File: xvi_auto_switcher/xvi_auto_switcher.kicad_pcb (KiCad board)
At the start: 2 copper layers, 45 x 102 mm, 20 parts, among them J1 DB37_Female_MountingHoles, J2 Conn_02x17_Odd_Even, J3 Conn_02x17_Odd_Even, J4 Conn_01x04_Male, J5 Conn_01x02_Male, U1 74LS157, U2 74LS07

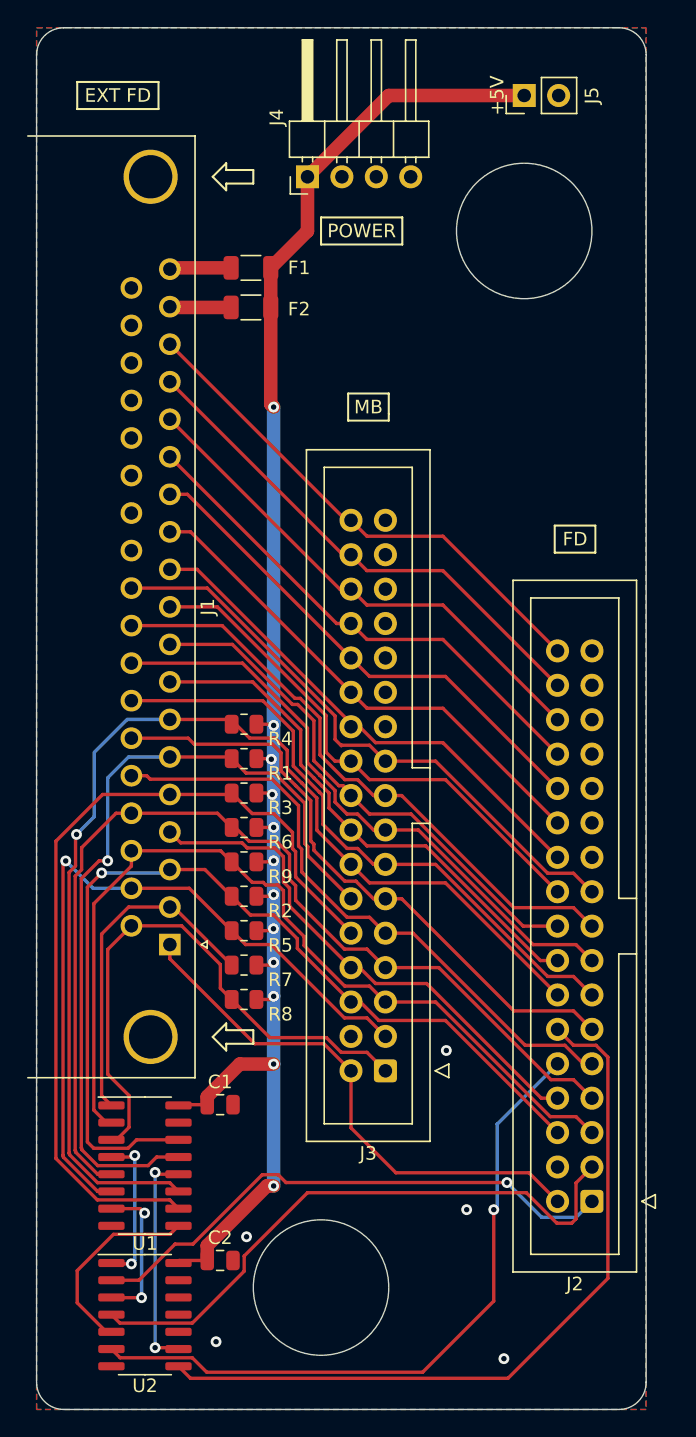
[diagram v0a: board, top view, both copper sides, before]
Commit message: update auto switcher pcb connector positions and add caps
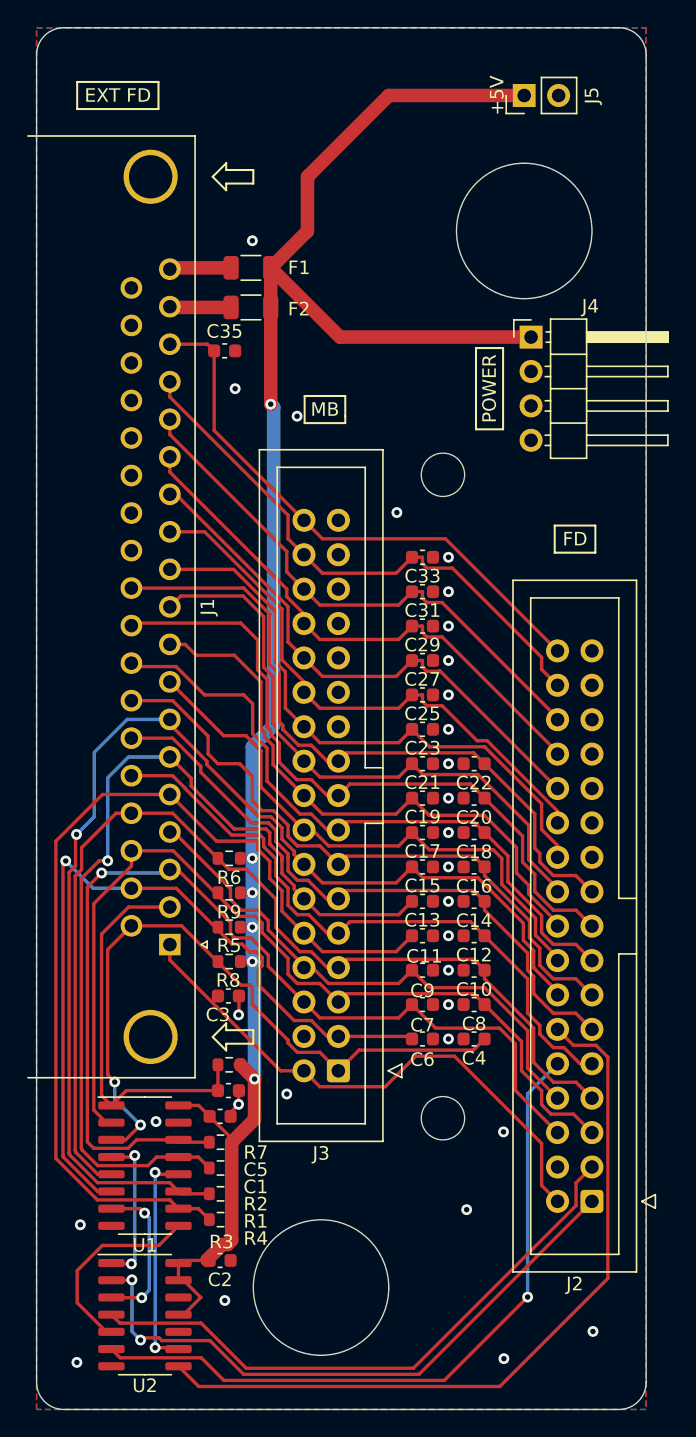
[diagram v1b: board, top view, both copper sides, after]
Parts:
- added C10: 47p, Capacitor_SMD:C_0603_1608Metric, F.Cu at (132.3, 129.6)
- added C11: 47p, Capacitor_SMD:C_0603_1608Metric, F.Cu at (128.5, 127.0)
- added C12: 47p, Capacitor_SMD:C_0603_1608Metric, F.Cu at (132.3, 127.0)
- added C13: 47p, Capacitor_SMD:C_0603_1608Metric, F.Cu at (128.5, 124.5)
- added C14: 47p, Capacitor_SMD:C_0603_1608Metric, F.Cu at (132.3, 124.5)
- added C15: 47p, Capacitor_SMD:C_0603_1608Metric, F.Cu at (128.5, 122.0)
- added C16: 47p, Capacitor_SMD:C_0603_1608Metric, F.Cu at (132.3, 122.0)
- added C17: 47p, Capacitor_SMD:C_0603_1608Metric, F.Cu at (128.5, 119.4)
- added C18: 47p, Capacitor_SMD:C_0603_1608Metric, F.Cu at (132.3, 119.4)
- added C19: 47p, Capacitor_SMD:C_0603_1608Metric, F.Cu at (128.5, 116.9)
- added C20: 47p, Capacitor_SMD:C_0603_1608Metric, F.Cu at (132.3, 116.9)
- added C21: 47p, Capacitor_SMD:C_0603_1608Metric, F.Cu at (128.5, 114.3)
- added C22: 47p, Capacitor_SMD:C_0603_1608Metric, F.Cu at (132.3, 114.3)
- added C23: 47p, Capacitor_SMD:C_0603_1608Metric, F.Cu at (128.5, 111.8)
- added C25: 47p, Capacitor_SMD:C_0603_1608Metric, F.Cu at (128.5, 109.2)
- added C27: 47p, Capacitor_SMD:C_0603_1608Metric, F.Cu at (128.5, 106.7)
- added C29: 47p, Capacitor_SMD:C_0603_1608Metric, F.Cu at (128.5, 104.2)
- added C3: 47p, Capacitor_SMD:C_0603_1608Metric, F.Cu at (114.2, 131.5)
- added C31: 47p, Capacitor_SMD:C_0603_1608Metric, F.Cu at (128.5, 101.6)
- added C33: 47p, Capacitor_SMD:C_0603_1608Metric, F.Cu at (128.5, 99.1)
- added C35: 47p, Capacitor_SMD:C_0603_1608Metric, F.Cu at (113.9, 83.8)
- added C4: 47p, Capacitor_SMD:C_0603_1608Metric, F.Cu at (132.3, 134.7)
- added C5: 47p, Capacitor_SMD:C_0603_1608Metric, F.Cu at (114.2, 138.5)
- added C6: 47p, Capacitor_SMD:C_0603_1608Metric, F.Cu at (128.5, 134.7)
- added C7: 47p, Capacitor_SMD:C_0603_1608Metric, F.Cu at (128.5, 132.1)
- added C8: 47p, Capacitor_SMD:C_0603_1608Metric, F.Cu at (132.3, 132.1)
- added C9: 47p, Capacitor_SMD:C_0603_1608Metric, F.Cu at (128.5, 129.6)
- added REF**: MountingHole_3.2mm_M3, MountingHole:MountingHole_3.2mm_M3, F.Cu at (130.0, 140.5)
- added REF**: MountingHole_3.2mm_M3, MountingHole:MountingHole_3.2mm_M3, F.Cu at (130.0, 93.0)
- C1, C2: footprint Capacitor_SMD:C_0805_2012Metric -> Capacitor_SMD:C_0603_1608Metric
- R1, R2, R3, R4, R5, R6, R7, R8, R9: footprint Resistor_SMD:R_0805_2012Metric -> Resistor_SMD:R_0603_1608Metric
- moved R4 34.7 mm to (113.6, 146.1)
- moved R3 31.5 mm to (113.6, 148.0)
- moved R1 30.3 mm to (113.6, 144.2)
- moved J4 20.3 mm to (136.5, 82.8), turned to 0 degrees
- moved R2 18.2 mm to (113.6, 142.3)
- moved R7 7.44 mm to (114.2, 136.6)
- moved J3 3.47 mm to (122.3, 137.0)
- moved R8 3.01 mm to (114.2, 128.9)
- moved R6 2.53 mm to (114.2, 121.3)
- moved R9 2.53 mm to (114.2, 123.9)
- moved R5 1.13 mm to (114.2, 126.4)
- moved C1 0.87 mm to (113.5, 140.4)
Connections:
- U2 pad 10: (no net) -> unconnected-(U2-Pad10)
- U2 pad 11: (no net) -> +5V
- U2 pad 12: (no net) -> unconnected-(U2-Pad12)
- U2 pad 13: (no net) -> +5V
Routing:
- net +5V: track 125.9 -> 141.4 mm, vias 12 -> 6
- net /~{OPTION0}: track 42.1 -> 51.4 mm, vias 0 -> 2
- net /~{DS0}: track 63.4 -> 71.6 mm
- net /~{DS1}: track 61.6 -> 69.2 mm
- net /~{WDATA}: track 37.6 -> 43.6 mm
- net /~{STEP}: track 38.9 -> 44.9 mm
- net /~{FDDINT}: track 44.3 -> 50.1 mm
- net /~{DS3}: track 69.7 -> 75.4 mm
- net /~{OPTION0_OUT}: track 40.5 -> 46.0 mm, vias 1 -> 2
- net /~{ERRDISK}: track 44.8 -> 50.3 mm
- net /~{WGATE}: track 37.5 -> 41.8 mm
- net /~{SWAP}: track 25.2 -> 29.0 mm
- net /~{DIR}: track 39.1 -> 42.9 mm
- net /~{DS2}: track 85.4 -> 89.2 mm
- net /~{OPTION1}: track 55.5 -> 59.1 mm
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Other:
- board text added: "ace/expert/super/xvi auto fd switcher v1.1 CERN-OHL-S 2023 https://github.com/tdaede/flux68k"
- board text added: "pin 18: +5V 250mA pin 19: +5V 250mA pin 2: L: internal 2-3 H: internal 0-1"
- board text removed: "ace/expert/super/xvi auto fd switcher v1.0 CERN-OHL-S 2023 https://github.com/tdaede/flux68k"
- board text removed: "pin 18: +5V 250mA pin 19: +5V 250mA pin 2: L: internal drives 2-3 H: internal drives 0-1"
